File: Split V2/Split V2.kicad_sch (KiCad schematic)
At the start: 63 parts, among them J1 AudioJack4

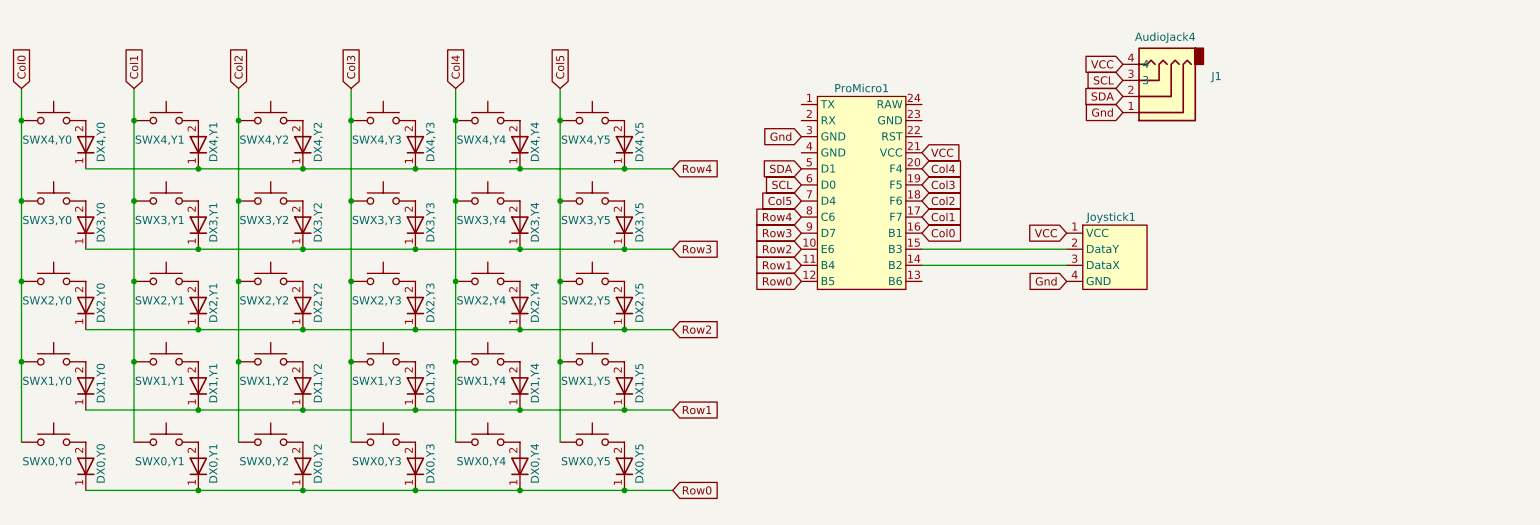
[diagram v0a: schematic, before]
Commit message: V1 Traces
Got all of my traces layed out and worked on creating the reversable footprint like in other projects. Need to do some more research as to the specifics
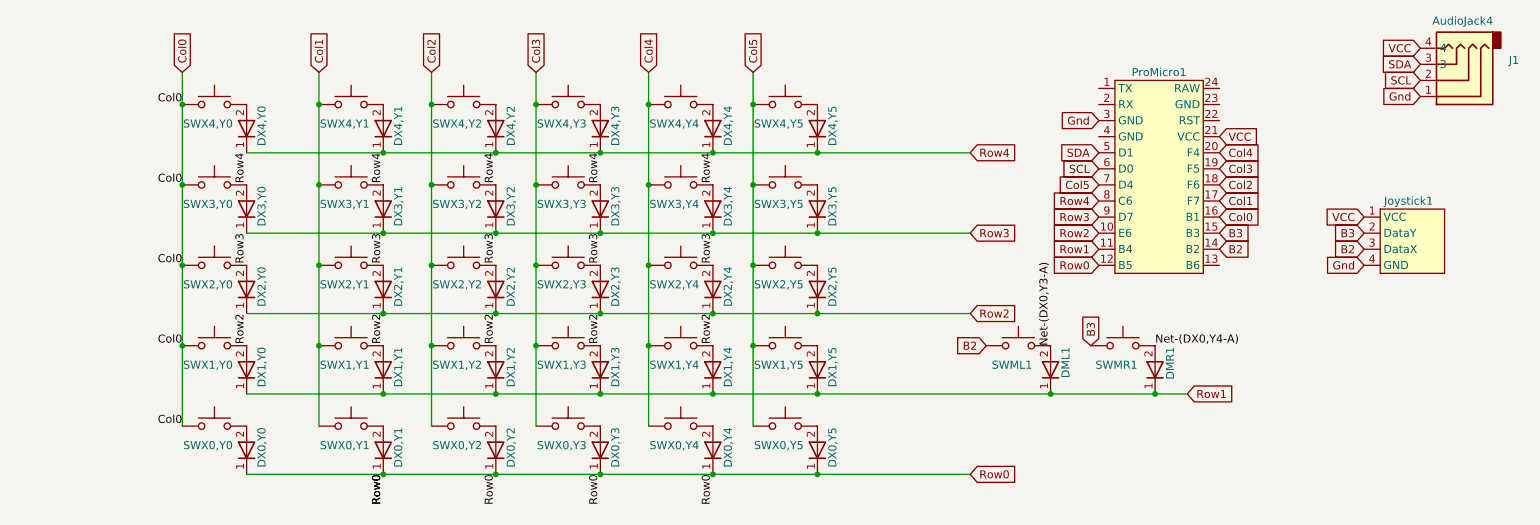
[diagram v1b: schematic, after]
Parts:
- removed DX0,Y5, DX1,Y5, DX2,Y5, DX3,Y5, DX4,Y5: ~, Custom:D_SOD-123_bothside, symbol Simulation_SPICE:D
- removed SWX0,Y5, SWX1,Y5, SWX2,Y5, SWX3,Y5, SWX4,Y5: ~, keyswitches.pretty-master:Kailh_socket_PG1350_optional_reversible, symbol Switch:SW_Push
- added DML1, DMR1, DX0,Y0, DX1,Y0, DX2,Y0, DX3,Y0, DX4,Y0: ~, Custom:D_SOD-123_bothside, symbol Simulation_SPICE:D
- added SWML1, SWMR1, SWX0,Y0, SWX1,Y0, SWX2,Y0, SWX3,Y0, SWX4,Y0: ~, keyswitches.pretty-master:Kailh_socket_PG1350_optional_reversible, symbol Switch:SW_Push
- renumbered DX0,Y0 to DX0,Y1, DX0,Y1 to DX0,Y2, DX0,Y2 to DX0,Y3, DX0,Y3 to DX0,Y4, DX0,Y4 to DX0,Y5, DX1,Y0 to DX1,Y1, DX1,Y1 to DX1,Y2, DX1,Y2 to DX1,Y3, DX1,Y3 to DX1,Y4, DX1,Y4 to DX1,Y5, DX2,Y0 to DX2,Y1, DX2,Y1 to DX2,Y2, DX2,Y2 to DX2,Y3, DX2,Y3 to DX2,Y4, DX2,Y4 to DX2,Y5, DX3,Y0 to DX3,Y1, DX3,Y1 to DX3,Y2, DX3,Y2 to DX3,Y3, DX3,Y3 to DX3,Y4, DX3,Y4 to DX3,Y5, DX4,Y0 to DX4,Y1, DX4,Y1 to DX4,Y2, DX4,Y2 to DX4,Y3, DX4,Y3 to DX4,Y4, DX4,Y4 to DX4,Y5, SWX0,Y0 to SWX0,Y1, SWX0,Y1 to SWX0,Y2, SWX0,Y2 to SWX0,Y3, SWX0,Y3 to SWX0,Y4, SWX0,Y4 to SWX0,Y5, SWX1,Y0 to SWX1,Y1, SWX1,Y1 to SWX1,Y2, SWX1,Y2 to SWX1,Y3, SWX1,Y3 to SWX1,Y4, SWX1,Y4 to SWX1,Y5, SWX2,Y0 to SWX2,Y1, SWX2,Y1 to SWX2,Y2, SWX2,Y2 to SWX2,Y3, SWX2,Y3 to SWX2,Y4, SWX2,Y4 to SWX2,Y5, SWX3,Y0 to SWX3,Y1, SWX3,Y1 to SWX3,Y2, SWX3,Y2 to SWX3,Y3, SWX3,Y3 to SWX3,Y4, SWX3,Y4 to SWX3,Y5, SWX4,Y0 to SWX4,Y1, SWX4,Y1 to SWX4,Y2, SWX4,Y2 to SWX4,Y3, SWX4,Y3 to SWX4,Y4, SWX4,Y4 to SWX4,Y5
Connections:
- net Col0: now also SWX0,Y0.1, SWX1,Y0.1, SWX2,Y0.1, SWX3,Y0.1, SWX4,Y0.1; no longer SWX0,Y1.1, SWX1,Y1.1, SWX2,Y1.1, SWX3,Y1.1, SWX4,Y1.1
- net Col1: now also SWX0,Y1.1, SWX1,Y1.1, SWX2,Y1.1, SWX3,Y1.1, SWX4,Y1.1; no longer SWX0,Y2.1, SWX1,Y2.1, SWX2,Y2.1, SWX3,Y2.1, SWX4,Y2.1
- net Col2: now also SWX0,Y2.1, SWX1,Y2.1, SWX2,Y2.1, SWX3,Y2.1, SWX4,Y2.1; no longer SWX0,Y3.1, SWX1,Y3.1, SWX2,Y3.1, SWX3,Y3.1, SWX4,Y3.1
- net Col3: now also SWX0,Y3.1, SWX1,Y3.1, SWX2,Y3.1, SWX3,Y3.1, SWX4,Y3.1; no longer SWX0,Y4.1, SWX1,Y4.1, SWX2,Y4.1, SWX3,Y4.1, SWX4,Y4.1
- net Col4: now also SWX0,Y4.1, SWX1,Y4.1, SWX2,Y4.1, SWX3,Y4.1, SWX4,Y4.1; no longer SWX0,Y5.1, SWX1,Y5.1, SWX2,Y5.1, SWX3,Y5.1, SWX4,Y5.1
- net Col5: now also SWX0,Y5.1, SWX1,Y5.1, SWX2,Y5.1, SWX3,Y5.1, SWX4,Y5.1
- net Row0: now also DX0,Y0.1 (K)
- net Row1: now also DML1.1 (K), DMR1.1 (K), DX1,Y0.1 (K)
- net Row2: now also DX2,Y0.1 (K)
- net Row3: now also DX3,Y0.1 (K)
- net Row4: now also DX4,Y0.1 (K)
- net SCL: now also J1.2; no longer J1.3
- net SDA: now also J1.3; no longer J1.2
- net B3: now reaches Joystick1.2 (DataY), ProMicro1.15 (B3)
- net B3: now also SWMR1.1
- net B2: now reaches Joystick1.3 (DataX), ProMicro1.14 (B2)
- net B2: now also SWML1.1
- new net: DX1,Y0.2 (A), SWX1,Y0.2
- new net: DX4,Y0.2 (A), SWX4,Y0.2
- new net: DX3,Y0.2 (A), SWX3,Y0.2
- new net: DX2,Y0.2 (A), SWX2,Y0.2
- new net: DX0,Y0.2 (A), SWX0,Y0.2
- new net Net-(DX0,Y3-A): DML1.2 (A), SWML1.2
- new net Net-(DX0,Y4-A): DMR1.2 (A), SWMR1.2
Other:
- moved on the sheet: DX0,Y1, DX0,Y2, DX0,Y3, DX0,Y4, DX0,Y5, DX1,Y1, DX1,Y2, DX1,Y3, DX1,Y4, DX1,Y5, DX2,Y1, DX2,Y2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

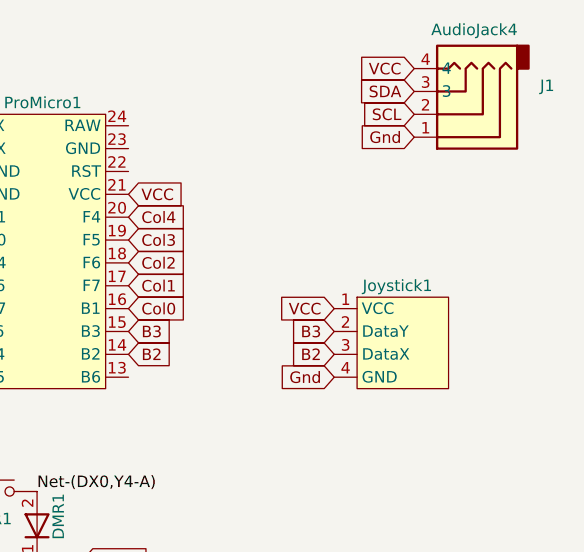
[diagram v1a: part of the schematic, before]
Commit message: Finished up double sided promicro
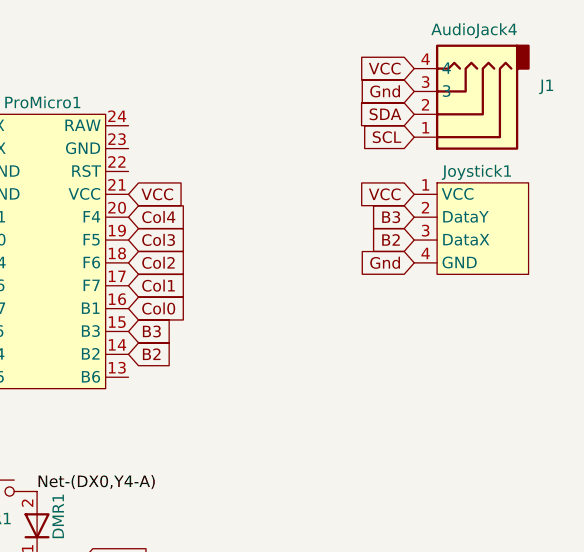
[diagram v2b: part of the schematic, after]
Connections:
- net Gnd: now also J1.3; no longer J1.1
- net SCL: now also J1.1; no longer J1.2
- net SDA: now also J1.2; no longer J1.3
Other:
- moved on the sheet: Joystick1

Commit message: Started new keyboard
Cad keyboard to companion with 3dconnexion mouse
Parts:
- SWML1, SWMR1, SWX0,Y0, SWX0,Y1, SWX0,Y2, SWX0,Y3, SWX0,Y4, SWX0,Y5, SWX1,Y0, SWX1,Y1, SWX1,Y2, SWX1,Y3, SWX1,Y4, SWX1,Y5, SWX2,Y0, SWX2,Y1, SWX2,Y2, SWX2,Y3, SWX2,Y4, SWX2,Y5, SWX3,Y0, SWX3,Y1, SWX3,Y2, SWX3,Y3, SWX3,Y4, SWX3,Y5, SWX4,Y0, SWX4,Y1, SWX4,Y2, SWX4,Y3, SWX4,Y4, SWX4,Y5: footprint keyswitches.pretty-master:Kailh_socket_PG1350_optional_reversible -> keyswitches.pretty-master:SW_MX_reversible
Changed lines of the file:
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@@
 			)
 		)
-		(property "Footprint" "keyswitches.pretty-master:Kailh_socket_PG1350_optional_reversible"
+		(property "Footprint" "keyswitches.pretty-master:SW_MX_reversible"
 			(at 88.9 52.07 0)
 			(effects
@@
 			)
 		)
-		(property "Footprint" "keyswitches.pretty-master:Kailh_socket_PG1350_optional_reversible"
+		(property "Footprint" "keyswitches.pretty-master:SW_MX_reversible"
 			(at 139.7 64.77 0)
 			(effects
@@
 			)
 		)
-		(property "Footprint" "keyswitches.pretty-master:Kailh_socket_PG1350_optional_reversible"
+		(property "Footprint" "keyswitches.pretty-master:SW_MX_reversible"
 			(at 71.12 52.07 0)
 			(effects
@@
 			)
 		)
-		(property "Footprint" "keyswitches.pretty-master:Kailh_socket_PG1350_optional_reversible"
+		(property "Footprint" "keyswitches.pretty-master:SW_MX_reversible"
 			(at 139.7 77.47 0)
 			(effects
@@
 			)
 		)
-		(property "Footprint" "keyswitches.pretty-master:Kailh_socket_PG1350_optional_reversible"
+		(property "Footprint" "keyswitches.pretty-master:SW_MX_reversible"
 			(at 123.19 77.47 0)
 			(effects
@@
 			)
 		)
-		(property "Footprint" "keyswitches.pretty-master:Kailh_socket_PG1350_optional_reversible"
+		(property "Footprint" "keyswitches.pretty-master:SW_MX_reversible"
 			(at 105.41 102.87 0)
 			(effects
@@
 			)
 		)
-		(property "Footprint" "keyswitches.pretty-master:Kailh_socket_PG1350_optional_reversible"
+		(property "Footprint" "keyswitches.pretty-master:SW_MX_reversible"
 			(at 123.19 102.87 0)
 			(effects
@@
 			)
 		)
-		(property "Footprint" "keyswitches.pretty-master:Kailh_socket_PG1350_optional_reversible"
+		(property "Footprint" "keyswitches.pretty-master:SW_MX_reversible"
 			(at 123.19 52.07 0)
 			(effects
@@
 			)
 		)
-		(property "Footprint" "keyswitches.pretty-master:Kailh_socket_PG1350_optional_reversible"
+		(property "Footprint" "keyswitches.pretty-master:SW_MX_reversible"
 			(at 105.41 77.47 0)
 			(effects
@@
 			)
 		)
-		(property "Footprint" "keyswitches.pretty-master:Kailh_socket_PG1350_optional_reversible"
+		(property "Footprint" "keyswitches.pretty-master:SW_MX_reversible"
 			(at 105.41 64.77 0)
 			(effects
@@
 			)
 		)
-		(property "Footprint" "keyswitches.pretty-master:Kailh_socket_PG1350_optional_reversible"
+		(property "Footprint" "keyswitches.pretty-master:SW_MX_reversible"
 			(at 105.41 90.17 0)
 			(effects
@@
 			)
 		)
-		(property "Footprint" "keyswitches.pretty-master:Kailh_socket_PG1350_optional_reversible"
+		(property "Footprint" "keyswitches.pretty-master:SW_MX_reversible"
 			(at 123.19 64.77 0)
 			(effects
@@
 			)
 		)
-		(property "Footprint" "keyswitches.pretty-master:Kailh_socket_PG1350_optional_reversible"
+		(property "Footprint" "keyswitches.pretty-master:SW_MX_reversible"
 			(at 49.53 52.07 0)
 			(effects
@@
 			)
 		)
-		(property "Footprint" "keyswitches.pretty-master:Kailh_socket_PG1350_optional_reversible"
+		(property "Footprint" "keyswitches.pretty-master:SW_MX_reversible"
 			(at 176.53 90.17 0)
 			(effects
@@
 			)
 		)
-		(property "Footprint" "keyswitches.pretty-master:Kailh_socket_PG1350_optional_reversible"
+		(property "Footprint" "keyswitches.pretty-master:SW_MX_reversible"
 			(at 71.12 102.87 0)
 			(effects
@@
 			)
 		)
-		(property "Footprint" "keyswitches.pretty-master:Kailh_socket_PG1350_optional_reversible"
+		(property "Footprint" "keyswitches.pretty-master:SW_MX_reversible"
 			(at 139.7 102.87 0)
 			(effects
@@
 			)
 		)
-		(property "Footprint" "keyswitches.pretty-master:Kailh_socket_PG1350_optional_reversible"
+		(property "Footprint" "keyswitches.pretty-master:SW_MX_reversible"
 			(at 105.41 52.07 0)
 			(effects
@@
 			)
 		)
-		(property "Footprint" "keyswitches.pretty-master:Kailh_socket_PG1350_optional_reversible"
+		(property "Footprint" "keyswitches.pretty-master:SW_MX_reversible"
 			(at 139.7 90.17 0)
 			(effects
@@
 			)
 		)
-		(property "Footprint" "keyswitches.pretty-master:Kailh_socket_PG1350_optional_reversible"
+		(property "Footprint" "keyswitches.pretty-master:SW_MX_reversible"
 			(at 49.53 64.77 0)
 			(effects
@@
 			)
 		)
-		(property "Footprint" "keyswitches.pretty-master:Kailh_socket_PG1350_optional_reversible"
+		(property "Footprint" "keyswitches.pretty-master:SW_MX_reversible"
 			(at 193.04 90.17 0)
 			(effects
@@
 			)
 		)
-		(property "Footprint" "keyswitches.pretty-master:Kailh_socket_PG1350_optional_reversible"
+		(property "Footprint" "keyswitches.pretty-master:SW_MX_reversible"
 			(at 88.9 64.77 0)
 			(effects
@@
 			)
 		)
-		(property "Footprint" "keyswitches.pretty-master:Kailh_socket_PG1350_optional_reversible"
+		(property "Footprint" "keyswitches.pretty-master:SW_MX_reversible"
 			(at 139.7 52.07 0)
 			(effects
@@
 			)
 		)
-		(property "Footprint" "keyswitches.pretty-master:Kailh_socket_PG1350_optional_reversible"
+		(property "Footprint" "keyswitches.pretty-master:SW_MX_reversible"
 			(at 88.9 77.47 0)
 			(effects
@@
 			)
 		)
-		(property "Footprint" "keyswitches.pretty-master:Kailh_socket_PG1350_optional_reversible"
+		(property "Footprint" "keyswitches.pretty-master:SW_MX_reversible"
 			(at 88.9 90.17 0)
 			(effects
@@
 			)
 		)
-		(property "Footprint" "keyswitches.pretty-master:Kailh_socket_PG1350_optional_reversible"
+		(property "Footprint" "keyswitches.pretty-master:SW_MX_reversible"
 			(at 49.53 102.87 0)
 			(effects
@@
 			)
 		)
-		(property "Footprint" "keyswitches.pretty-master:Kailh_socket_PG1350_optional_reversible"
+		(property "Footprint" "keyswitches.pretty-master:SW_MX_reversible"
 			(at 71.12 64.77 0)
 			(effects
@@
 			)
 		)
-		(property "Footprint" "keyswitches.pretty-master:Kailh_socket_PG1350_optional_reversible"
+		(property "Footprint" "keyswitches.pretty-master:SW_MX_reversible"
 			(at 123.19 90.17 0)
 			(effects
@@
 			)
 		)
-		(property "Footprint" "keyswitches.pretty-master:Kailh_socket_PG1350_optional_reversible"
+		(property "Footprint" "keyswitches.pretty-master:SW_MX_reversible"
 			(at 71.12 77.47 0)
 			(effects
@@
 			)
 		)
-		(property "Footprint" "keyswitches.pretty-master:Kailh_socket_PG1350_optional_reversible"
+		(property "Footprint" "keyswitches.pretty-master:SW_MX_reversible"
 			(at 49.53 90.17 0)
 			(effects
@@
 			)
 		)
-		(property "Footprint" "keyswitches.pretty-master:Kailh_socket_PG1350_optional_reversible"
+		(property "Footprint" "keyswitches.pretty-master:SW_MX_reversible"
 			(at 88.9 102.87 0)
 			(effects
@@
 			)
 		)
-		(property "Footprint" "keyswitches.pretty-master:Kailh_socket_PG1350_optional_reversible"
+		(property "Footprint" "keyswitches.pretty-master:SW_MX_reversible"
 			(at 49.53 77.47 0)
 			(effects
@@
 			)
 		)
-		(property "Footprint" "keyswitches.pretty-master:Kailh_socket_PG1350_optional_reversible"
+		(property "Footprint" "keyswitches.pretty-master:SW_MX_reversible"
 			(at 71.12 90.17 0)
 			(effects
